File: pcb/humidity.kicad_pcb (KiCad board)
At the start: 2 copper layers, 59.7 x 27.9 mm, 16 parts, among them J1 Battery Holder, J2 Conn_01x09, J3 Conn_02x09_Odd_Even, SW1 SW_Push, U1 BME280, U2 ESP32-WROOM-32

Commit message: pcb: Update to use SHT-31 humidity chip
Replace bme280 with sht31 humidity chip.

Add jlcpcb tooling holes to the board.

Save gerber files to pcb/out/ directory.

Signed-off-by: Kevin O'Connor <kevin@koconnor.net>
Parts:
- removed C1: 100nF, Capacitor_SMD:C_0402_1005Metric
- R1: value 10K -> 10K Ohm
- R2, R3: value 4K7 -> 4.7K Ohm
- R4: value 0K1 -> 100 Ohm
- U1: value BME280 -> SHT31-DIS; footprint Package_LGA:Bosch_LGA-8_2.5x2.5mm_P0.65mm_ClockwisePinNumbering -> Sensor_Humidity:Sensirion_DFN-8-1EP_2.5x2.5mm_P0.5mm_EP1.1x1.7mm
- moved R3 1.78 mm to (176.5, 127.2), turned to 0 degrees
- moved C3 1.25 mm to (177.8, 134.5)
- moved U1 0.07 mm to (178.7, 131.3), turned to 270 degrees
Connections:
- R2 pad 2: SCL -> SDA
- R3 pad 2: SDA -> SCL
- U1 pad 1: GND -> SDA
- U1 pad 2: +BATT -> GND
- U1 pad 3: SDA -> Net-(U1-Pad3)
- U1 pad 6: +BATT -> Net-(U1-Pad6)
- U1 pad 8: +BATT -> GND
- U2 pad 36: SDA -> SCL
- U2 pad 37: SCL -> SDA
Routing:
- net GND: track 9.85 -> 20.5 mm
- net SCL: track 9.02 -> 12.8 mm
- net +BATT: track 82.2 -> 78.9 mm
- net SDA: track 11.9 -> 9.55 mm
- net (no net): vias 0 -> 3
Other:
- board text added: "Humidity v0.6s"
- board text removed: "Humidity v0.6"

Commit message: pcb: Add mains powered variant of board
Add usb-micro-b connector for power and comms.

Add ams1117-3.3v regulator for power.

Add ch340 chip for comms.

Signed-off-by: Kevin O'Connor <kevin@koconnor.net>
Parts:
- added C1: 22uF, Capacitor_SMD:C_0805_2012Metric, F.Cu at (157.0, 114.9)
- added C6: 22uF, Capacitor_SMD:C_0805_2012Metric, F.Cu at (168.4, 110.8)
- added C7: 100nF, Capacitor_SMD:C_0402_1005Metric, F.Cu at (163.3, 121.2)
- added C8: 100nF, Capacitor_SMD:C_0402_1005Metric, F.Cu at (163.3, 118.9)
- added REF**: tooling hole, pcb:tooling hole, F.Cu at (152.5, 124.0)
- added REF**: tooling hole, pcb:tooling hole, F.Cu at (152.5, 110.5)
- added REF**: tooling hole, pcb:tooling hole, F.Cu at (208.5, 134.5)
- added U3: AMS1117-3.3, Package_TO_SOT_SMD:SOT-223-3_TabPin2, F.Cu at (162.8, 113.2)
- added U4: CH340E, Package_SO:MSOP-10_3x3mm_P0.5mm, F.Cu at (159.1, 120.3)
- J1: value Battery Holder -> USB_B_Micro; footprint Battery:BatteryHolder_Keystone_2460_1xAA -> Connector_USB:USB_Micro-B_Amphenol_10118194_Horizontal; moved to F.Cu
- moved J1 53.1 mm to (152.6, 117.8), turned to 270 degrees
- moved SW1 10.5 mm to (174.4, 118.5)
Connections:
- J1 pad 1: +BATT -> Net-(C1-Pad1)
- J1 pad 2: GND -> USB_DM
- U1 pad 3: Net-(U1-Pad3) -> (no net)
- U1 pad 6: Net-(U1-Pad6) -> (no net)
- U2 pad 17: Net-(U2-Pad17) -> (no net)
- U2 pad 18: Net-(U2-Pad18) -> (no net)
- U2 pad 19: Net-(U2-Pad19) -> (no net)
- U2 pad 20: Net-(U2-Pad20) -> (no net)
- U2 pad 21: Net-(U2-Pad21) -> (no net)
- U2 pad 22: Net-(U2-Pad22) -> (no net)
- U2 pad 23: Net-(U2-Pad23) -> (no net)
- U2 pad 32: Net-(U2-Pad32) -> (no net)
- U2 pad 4: Net-(U2-Pad4) -> (no net)
- U2 pad 5: Net-(U2-Pad5) -> (no net)
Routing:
- net +BATT: track 78.9 -> 143.5 mm, vias 1 -> 3
- net TXD: track 25.9 -> 63.5 mm, vias 0 -> 2
- net RXD: track 29.0 -> 63.2 mm, vias 0 -> 2
- net GND: track 20.5 -> 30.9 mm, vias 28 -> 30
- net USB_DM: track 0.00 -> 6.55 mm
- net Net-(C1-Pad1): track 0.00 -> 6.02 mm
- net USB_DP: track 0.00 -> 2.94 mm
- net IO2: track 45.8 -> 44.2 mm
- net BOOT: track 47.5 -> 46.4 mm
- net Net-(U2-Pad4): track 0.87 -> 0.00 mm
- net Net-(U2-Pad5): track 0.82 -> 0.00 mm
- net (no net): vias 3 -> 2
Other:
- board text added: "Humidity v0.6m"
- board text removed: "3.2V Lifepo4 ONLY"
- board text removed: "Humidity v0.6s"

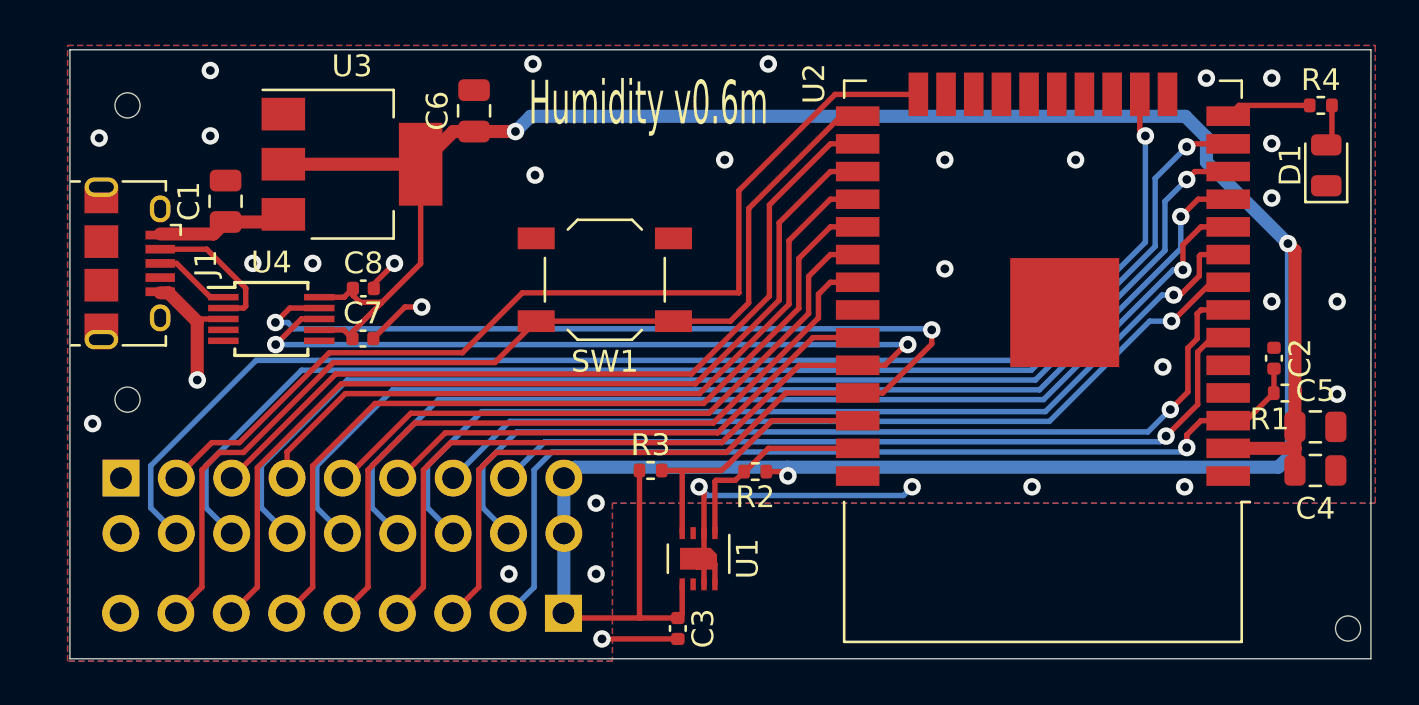
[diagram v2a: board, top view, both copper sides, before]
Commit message: pcb: WIP - convert to an ht7833 regulator
Signed-off-by: Kevin O'Connor <kevin@koconnor.net>
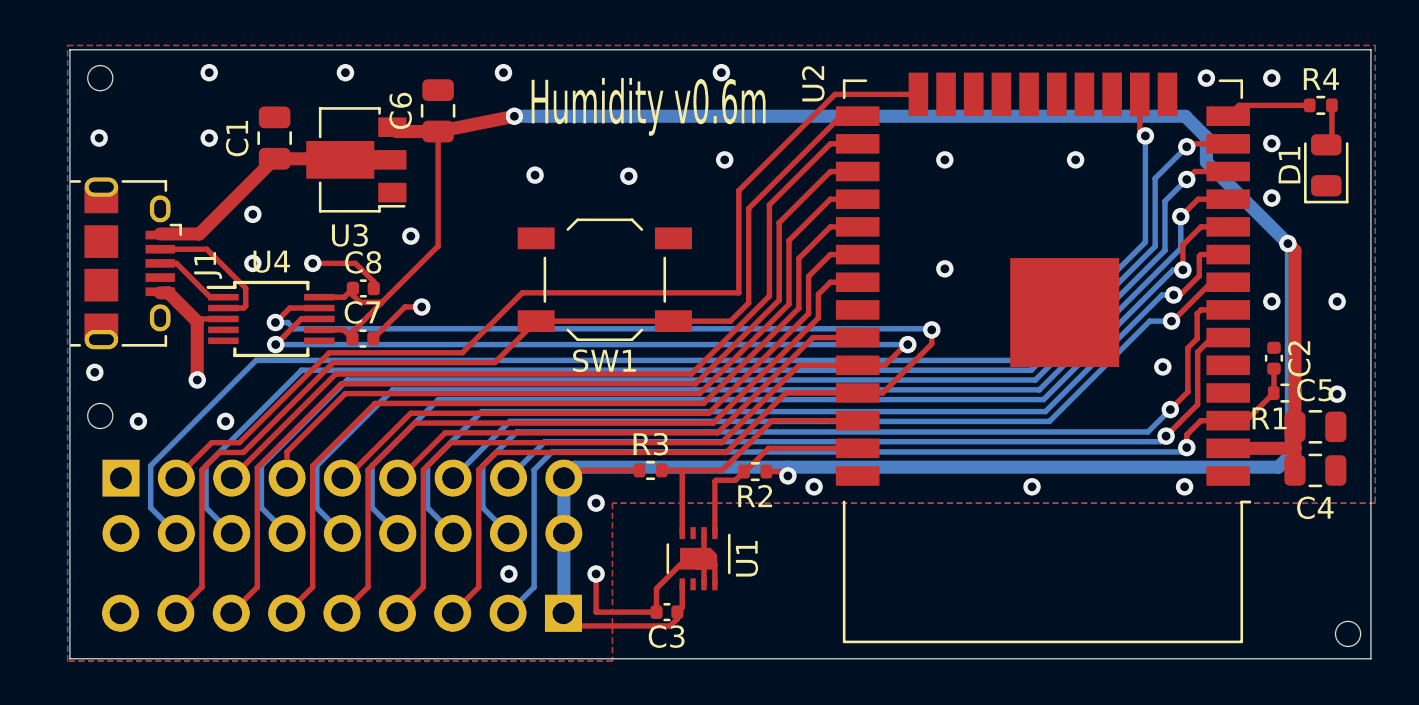
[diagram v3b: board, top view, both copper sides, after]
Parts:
- removed REF** (x3): tooling hole, pcb:tooling hole
- added H1: ToolingHole, pcb:tooling_hole, F.Cu at (208.5, 134.8)
- added H2: ToolingHole, pcb:tooling_hole, F.Cu at (151.2, 109.2)
- added H3: ToolingHole, pcb:tooling_hole, F.Cu at (151.2, 124.8)
- C1, C6: value 22uF -> 10uF
- U3: value AMS1117-3.3 -> HT7833-1-SOT89; footprint Package_TO_SOT_SMD:SOT-223-3_TabPin2 -> Package_TO_SOT_SMD:SOT-89-3
- moved C1 3.67 mm to (159.2, 112.0)
- moved C6 1.65 mm to (166.8, 110.8)
- moved C3 0.90 mm to (177.2, 133.8), turned to 180 degrees
- moved U3 0.28 mm to (163.0, 113.0), turned to 180 degrees
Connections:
- U3 pad 2: +BATT -> Net-(C1-Pad1)
- U3 pad 3: Net-(C1-Pad1) -> +BATT
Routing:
- net +BATT: track 143.5 -> 136.7 mm
- net GND: track 30.9 -> 24.9 mm, vias 30 -> 35
- net Net-(C1-Pad1): track 6.02 -> 12.0 mm
- net (no net): vias 2 -> 0
